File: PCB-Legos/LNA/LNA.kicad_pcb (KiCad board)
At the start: 4 copper layers, 50.8 x 27.9 mm, 36 parts, among them J1 Conn_Coaxial, J2 Conn_Coaxial, J3 Conn_Coaxial, U1 LP2985XX-N, U2 LNA-TP3M9037, U3 QPQ1907, U4 LP2985XX-N, U5 LNA-TP3M9037, U6 QPQ1907

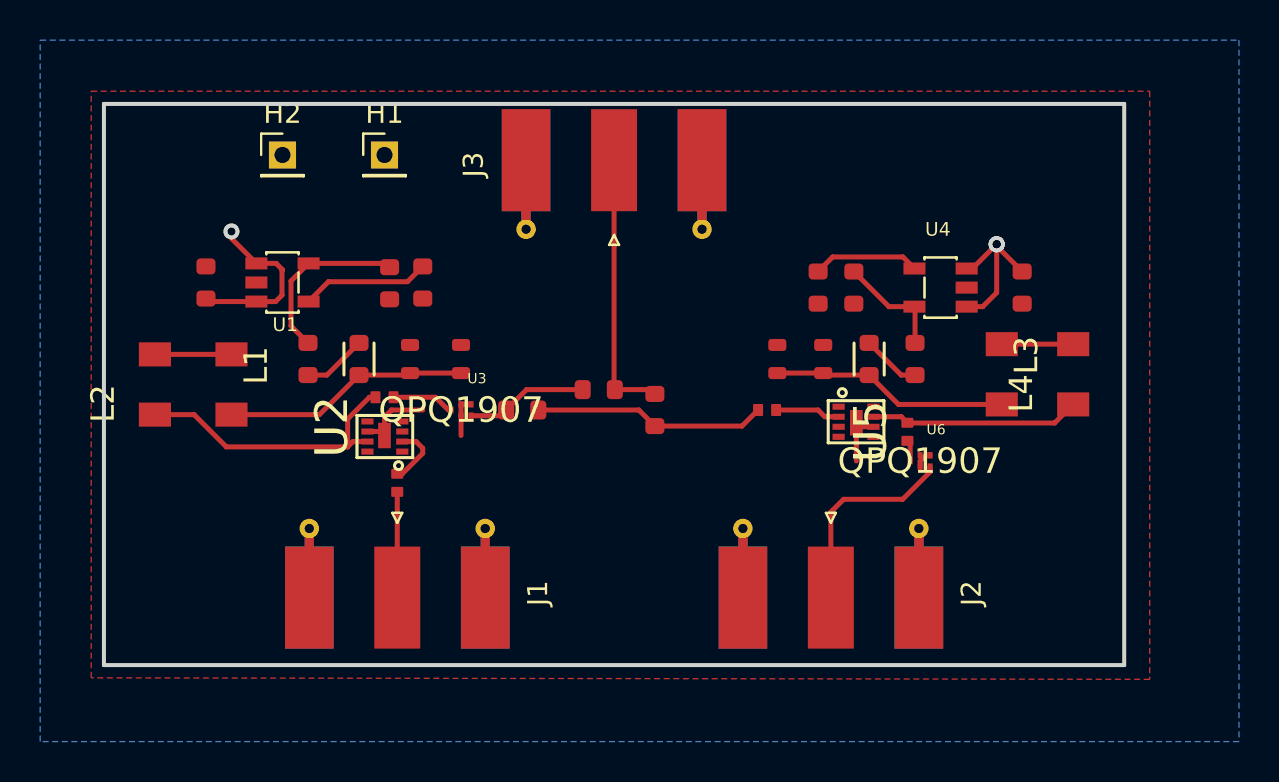
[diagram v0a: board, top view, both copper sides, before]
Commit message: LNA Test Board
LNA Test Board. Has ability to test each stage separately.
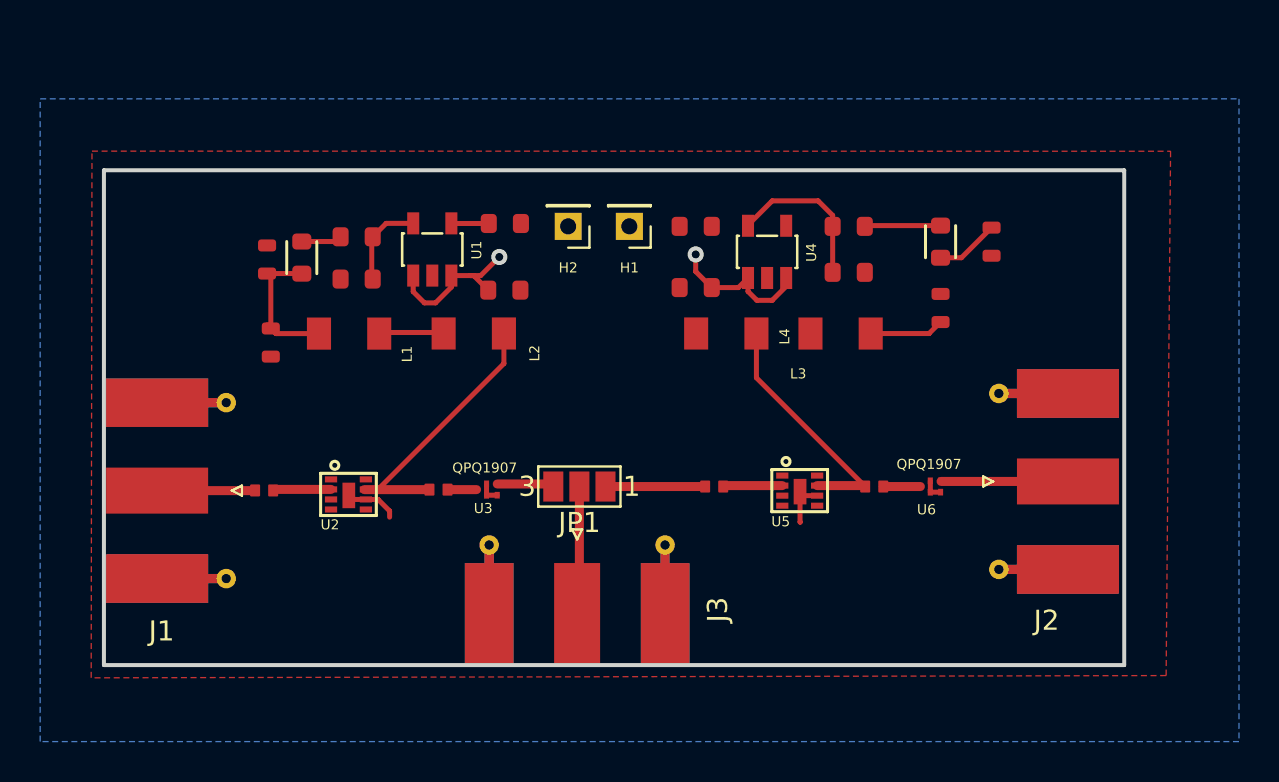
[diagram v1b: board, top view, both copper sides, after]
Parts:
- removed R3, R4, R5: 0, HGS_Reflector:.0603-B-NOSILK
- added JP1: SolderJumper_3_Open, Jumper:SolderJumper-3_P1.3mm_Open_Pad1.0x1.5mm_NumberLabels, F.Cu at (135.4, 82.5)
- moved J3 19.2 mm to (135.3, 87.2), turned to 90 degrees
- moved L4 17.4 mm to (142.7, 74.9), turned to 180 degrees
- moved C3 16.3 mm to (141.2, 72.6), turned to 0 degrees
- moved L2 16.1 mm to (130.2, 74.9), turned to 180 degrees
- moved C10 14.9 mm to (131.7, 72.8), turned to 180 degrees
- moved H2 14.7 mm to (134.9, 69.6), turned to 180 degrees
- moved H1 12.7 mm to (137.9, 69.6), turned to 180 degrees
- moved C14 12.2 mm to (156.0, 70.4), turned to -90 degrees
- moved J2 10.9 mm to (158.0, 82.3), turned to 180 degrees
- moved C7 10.9 mm to (119.9, 71.2)
- moved J1 10.9 mm to (116.1, 82.8), turned to 0 degrees
- moved U4 8.82 mm to (144.8, 70.9), turned to 90 degrees
- moved L3 8.28 mm to (148.4, 74.9), turned to 0 degrees
- moved U1 7.64 mm to (128.1, 70.7), turned to 90 degrees
- moved R2 7.38 mm to (148.8, 69.6), turned to 0 degrees
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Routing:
- net Net-(J3-Pad1): track 13.5 -> 6.40 mm
- net Net-(C9-Pad1): track 11.6 -> 4.96 mm
- net Net-(C11-Pad1): track 5.33 -> 0.00 mm
- net Net-(C7-Pad1): track 12.3 -> 7.31 mm
- net Net-(C14-Pad1): track 11.8 -> 6.88 mm
- net Net-(C4-Pad1): track 6.41 -> 1.87 mm
- net Net-(C5-Pad1): track 8.78 -> 4.59 mm
- net Net-(J2-Pad1): track 10.3 -> 6.35 mm
- net Net-(L3-Pad1): track 3.56 -> 0.00 mm
- net Net-(U3-PadOUTPUT): track 6.10 -> 2.84 mm
- net GND: track 9.69 -> 7.31 mm
- net Net-(C12-Pad1): track 5.56 -> 7.88 mm
- net Net-(C13-Pad1): track 10.5 -> 12.3 mm
- net Net-(C6-Pad2): track 2.99 -> 1.45 mm
- net VUSB: track 16.9 -> 15.3 mm, vias 3 -> 2
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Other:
- board size 50.8 x 27.9 mm -> 50.8 x 24.6 mm

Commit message: LNA Board
LNA Test board with ability to test each stage
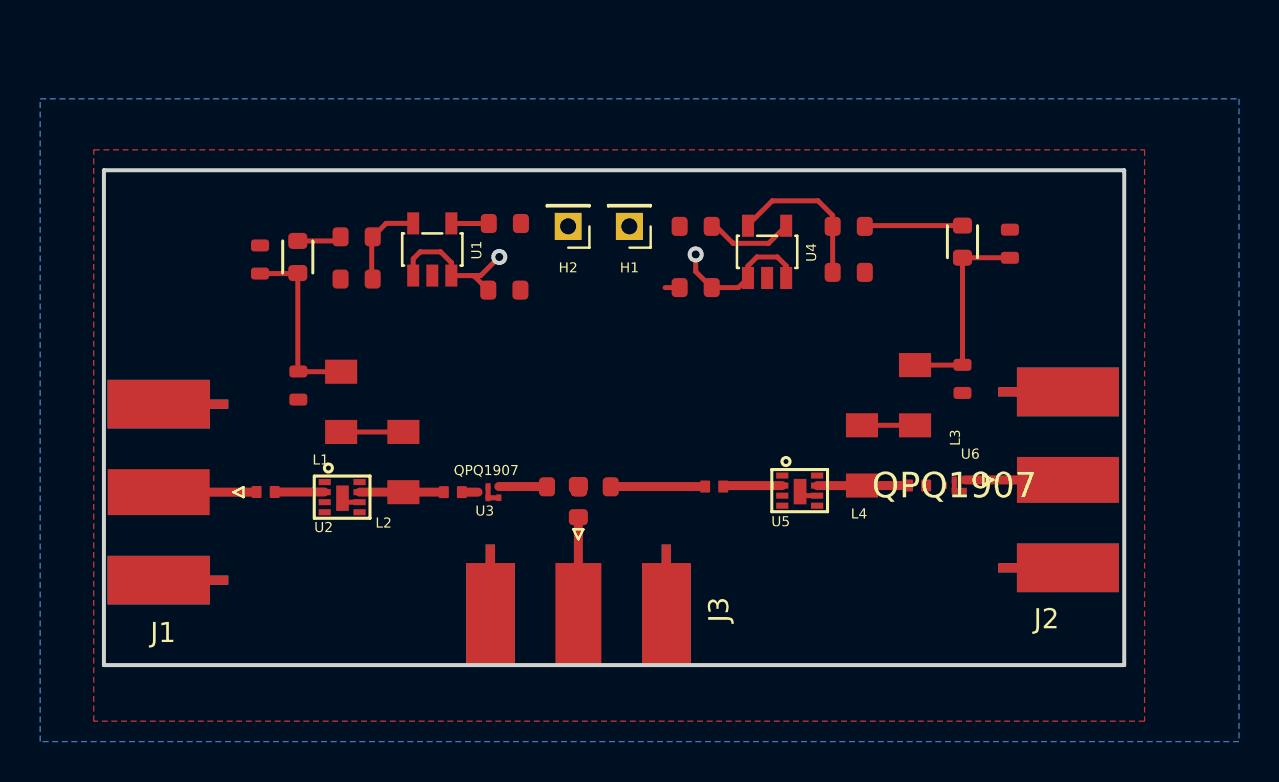
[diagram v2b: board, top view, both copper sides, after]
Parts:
- removed JP1: SolderJumper_3_Open, Jumper:SolderJumper-3_P1.3mm_Open_Pad1.0x1.5mm_NumberLabels
- added R3: 0, HGS_Reflector:.0603-B-NOSILK, F.Cu at (134.6, 82.6)
- added R4: 0, HGS_Reflector:.0603-B-NOSILK, F.Cu at (135.4, 83.3)
- added R5: 0, HGS_Reflector:.0603-B-NOSILK, F.Cu at (136.2, 82.6)
- moved L4 9.08 mm to (149.5, 81.0), turned to 90 degrees
- moved L2 7.30 mm to (126.7, 81.3), turned to 90 degrees
- moved L3 4.81 mm to (152.1, 78.0), turned to 90 degrees
- moved C15 3.70 mm to (154.5, 77.2), turned to -90 degrees
- moved L1 3.42 mm to (123.6, 78.3), turned to 90 degrees
- moved C8 2.54 mm to (121.4, 77.5)
- moved C13 2.13 mm to (152.2, 82.5)
- moved U6 1.19 mm to (154.1, 82.5)
- moved E2 1.09 mm to (154.5, 70.4)
- moved C14 0.92 mm to (156.9, 70.5), turned to 90 degrees
- moved C6 0.73 mm to (129.1, 82.8)
- moved C7 0.35 mm to (119.5, 71.2)
- moved U2 0.34 mm to (123.6, 83.1)
- moved E1 0.20 mm to (121.4, 71.1)
- moved U3 0.15 mm to (130.9, 82.8)
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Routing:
- net Net-(C6-Pad1): track 14.3 -> 4.20 mm
- net Net-(C13-Pad1): track 12.3 -> 4.53 mm
- net Net-(C11-Pad1): track 0.00 -> 4.42 mm
- net Net-(C14-Pad1): track 6.88 -> 10.1 mm
- net Net-(L3-Pad1): track 0.00 -> 2.64 mm
- net GND: track 7.31 -> 4.93 mm
- net Net-(C13-Pad2): track 1.85 -> 0.00 mm
- net Net-(C7-Pad1): track 7.31 -> 8.94 mm
- net Net-(J3-Pad1): track 6.40 -> 5.05 mm
- net Net-(J2-Pad1): track 6.35 -> 5.15 mm
- net Net-(E2-Pad1): track 3.79 -> 4.88 mm
- net Net-(C6-Pad2): track 1.45 -> 0.81 mm
- net Net-(E1-Pad1): track 2.03 -> 2.55 mm

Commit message: LNA Test Board
LNA test board with ability to test each of two stages.
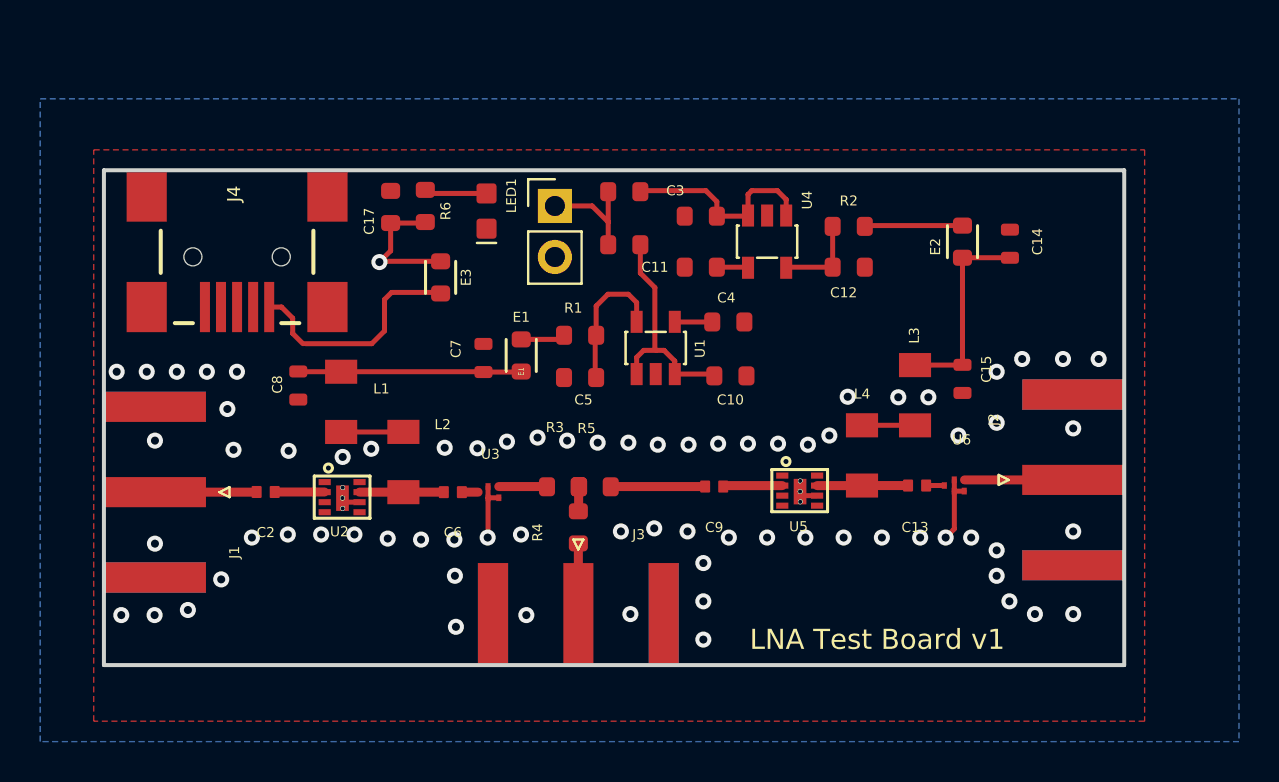
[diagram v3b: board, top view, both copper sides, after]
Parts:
- removed H1: GND, Connector_PinHeader_2.00mm:PinHeader_1x01_P2.00mm_Vertical
- added C17: 1 uF, HGS_Reflector:.0603-B-NOSILK, F.Cu at (126.0, 68.6)
- added E3: BLM18DN381SZ1D, HGS_Reflector:.0603-B, F.Cu at (128.5, 72.1)
- added J4: 474-PRT-00587, HGS_Reflector:USB-MINIB, F.Cu at (118.4, 71.1)
- added LED1: GREEN, HGS_Reflector:LED-0603, F.Cu at (130.8, 68.8)
- added R6: 1k, HGS_Reflector:.0603-B-NOSILK, F.Cu at (127.8, 68.6)
- added R7: 0, HGS_Reflector:.0603-B-NOSILK, F.Cu at (137.7, 67.9)
- added R8: 0, HGS_Reflector:.0603-B-NOSILK, F.Cu at (137.7, 70.5)
- H2: footprint Connector_PinHeader_2.00mm:PinHeader_1x01_P2.00mm_Vertical -> Connector_PinHeader_2.54mm:PinHeader_1x02_P2.54mm_Vertical
- J1, J2, J3: footprint Connector_Coaxial:SMA_Molex_73251-1153_EdgeMount_Horizontal -> Connector_Coaxial:SMA_Amphenol_132289_EdgeMount
- moved C4 12.2 mm to (142.8, 74.4)
- moved C7 12.2 mm to (130.7, 76.1)
- moved E1 12.2 mm to (132.5, 76.0)
- moved U1 12.2 mm to (139.2, 75.7)
- moved C5 12.2 mm to (135.5, 77.1)
- moved R1 12.2 mm to (135.5, 75.0)
- moved C10 12.0 mm to (143.0, 77.0)
- moved C3 3.57 mm to (141.5, 69.1)
- moved C11 2.05 mm to (141.5, 71.6)
- moved J2 1.98 mm to (160.0, 82.2), turned to 0 degrees
- moved J1 1.91 mm to (114.3, 82.8), turned to 180 degrees
- moved J3 1.72 mm to (135.4, 88.9), turned to -90 degrees
- moved R4 1.31 mm to (135.4, 84.6)
- moved H2 1.21 mm to (134.2, 68.6), turned to 0 degrees
- moved U4 0.51 mm to (144.8, 70.4), turned to -90 degrees
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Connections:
- C10 pad 2: VUSB -> Net-(C10-Pad2)
- C3 pad 2: VUSB -> Net-(C3-Pad2)
- U1 pad 1: VUSB -> Net-(C3-Pad2)
- U1 pad 3: VUSB -> Net-(C3-Pad2)
- U2 pad 2X2_DFN_8PIN2: Net-(C2-Pad2) -> (no net)
- U2 pad 2X2_DFN_8PIN6: GND -> (no net)
- U2 pad 2X2_DFN_8PIN7: Net-(C6-Pad1) -> (no net)
- U2 pad P$1: GND -> (no net)
- U4 pad 1: VUSB -> Net-(C10-Pad2)
- U4 pad 3: VUSB -> Net-(C10-Pad2)
- U5 pad 2X2_DFN_8PIN2: Net-(C9-Pad2) -> (no net)
- U5 pad 2X2_DFN_8PIN6: GND -> (no net)
- U5 pad 2X2_DFN_8PIN7: Net-(C13-Pad1) -> (no net)
- U5 pad P$1: GND -> (no net)
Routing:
- net Net-(E3-Pad1): track 0.00 -> 11.6 mm
- net Net-(C3-Pad2): track 0.00 -> 11.3 mm
- net Net-(C10-Pad2): track 0.00 -> 10.4 mm
- net GND: track 4.93 -> 8.71 mm, vias 0 -> 79
- net Net-(C12-Pad1): track 7.88 -> 4.36 mm
- net Net-(LED1-PadA): track 0.00 -> 3.37 mm
- net VUSB: track 15.7 -> 12.6 mm, vias 2 -> 1
- net Net-(C11-Pad1): track 4.42 -> 1.56 mm
- net Net-(C5-Pad1): track 4.59 -> 7.14 mm
- net Net-(C7-Pad1): track 8.94 -> 11.2 mm
- net Net-(R3-Pad2): track 0.00 -> 1.22 mm
- net Net-(C13-Pad2): track 0.00 -> 0.91 mm
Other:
- board text added: "E1"
- board text added: "KK7AQM teehee"
- board text added: "LNA Test Board v1"

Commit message: LNA Test Board
PCB to test each stage ofthe HGS LNA
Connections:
- J4 pad S1: Net-(J4-PadS1) -> GND
- J4 pad S2: Net-(J4-PadS1) -> GND
- J4 pad S3: Net-(J4-PadS1) -> GND
- J4 pad S4: Net-(J4-PadS1) -> GND
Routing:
- net GND: vias 79 -> 102
